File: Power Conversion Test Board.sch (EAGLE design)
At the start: 44 parts, among them U1 LM2678, U2 LM2678

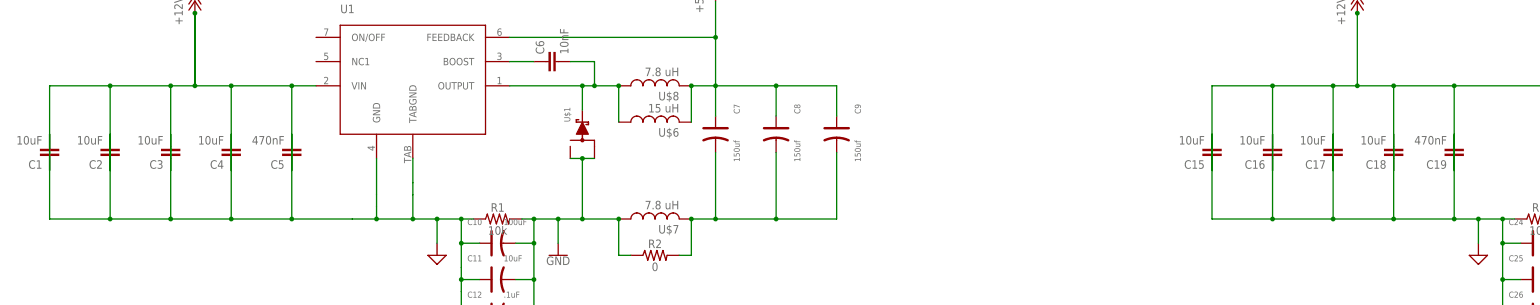
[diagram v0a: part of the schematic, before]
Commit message: Changed schematic layout and starting routing
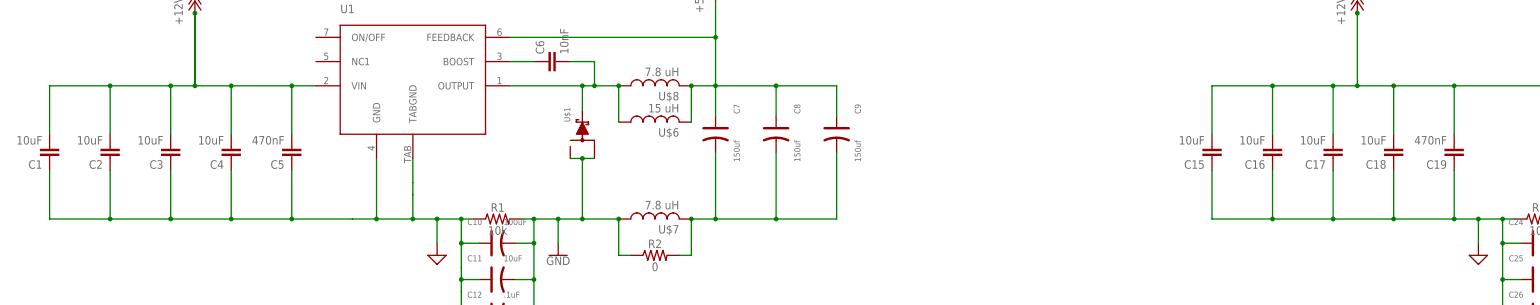
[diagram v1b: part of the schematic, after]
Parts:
- C1, C15, C16, C17, C18, C2, C3, C4: device SparkFun-Capacitors:10UF-0603-6.3V-20% -> SparkFun-Capacitors:10UF-1206-6.3V-20%
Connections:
- net +12V: now also C1.2, C15.2, C16.2, C17.2, C18.2, C19.2, C2.2, C3.2, C4.2, C5.2; no longer C1.1, C15.1, C16.1, C17.1, C18.1, C19.1, C2.1, C3.1, C4.1, C5.1
- net GND: now also C1.1, C15.1, C16.1, C17.1, C18.1, C19.1, C2.1, C3.1, C4.1, C5.1; no longer C1.2, C15.2, C16.2, C17.2, C18.2, C19.2, C2.2, C3.2, C4.2, C5.2

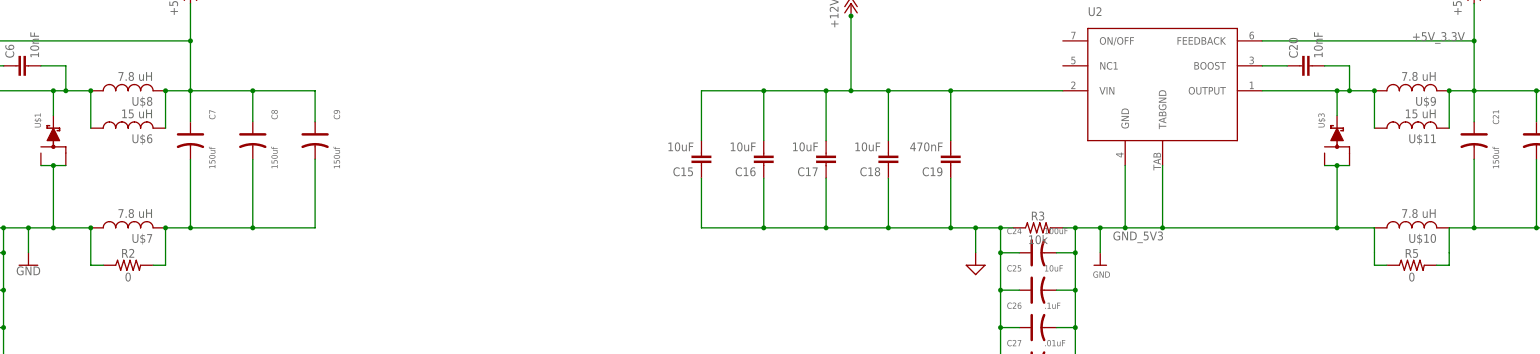
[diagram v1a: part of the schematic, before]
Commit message: Rerouting
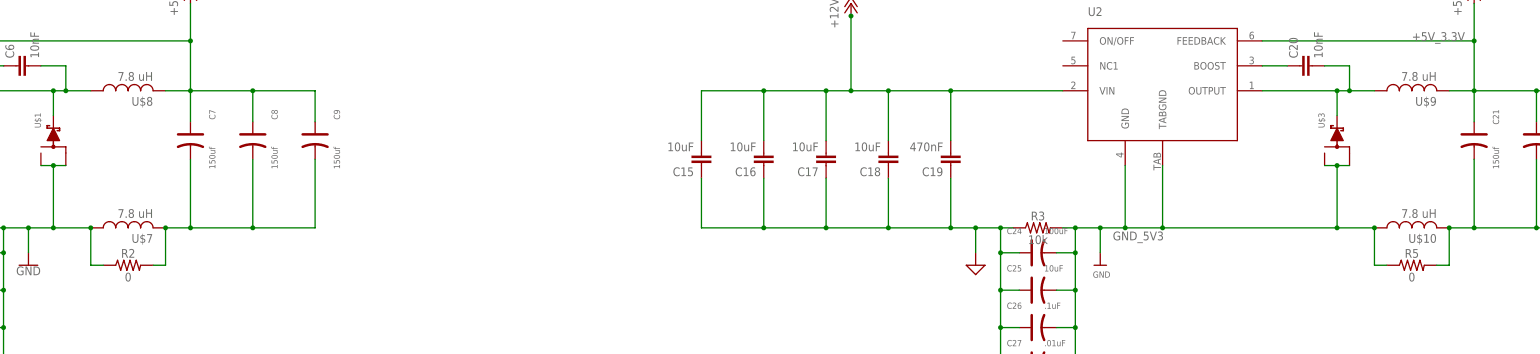
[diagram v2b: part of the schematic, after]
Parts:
- removed U$11, U$6: 15 uH, DiscreteComponents:HCMA1305
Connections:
- removed net GND_5V1: R5.1
- removed net N$6: C21.-, C22.-, C23.-, U$10.2
- net +5V: no longer U$6.2
- net +5V_3.3V: no longer U$11.2
- net GND_5V3: now also R5.1
- net N$1: no longer U$6.1
- net N$4: now also C21.-, C22.-, C23.-, U$10.2
- net N$7: no longer U$11.1
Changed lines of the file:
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@@
 <part name="U$2" library="microbuilder" deviceset="GND" device=""/>
 <part name="R2" library="SparkFun-Resistors" library_urn="urn:adsk.eagle:library:532" deviceset="RESISTOR" device="0603" package3d_urn="urn:adsk.eagle:package:39650/1" value="0"/>
-<part name="R5" library="SparkFun-Resistors" library_urn="urn:adsk.eagle:library:532" deviceset="RESISTOR" device="0603" package3d_urn="urn:adsk.eagle:package:39650/1" value="0"/>
 <part name="U$5" library="board_outlines" deviceset="BOARD" device="PCB"/>
 <part name="U$8" library="DiscreteComponents" deviceset="HCMA1305" device="" value="7.8 uH"/>
 <part name="U$9" library="DiscreteComponents" deviceset="HCMA1305" device="" value="7.8 uH"/>
 <part name="U$10" library="DiscreteComponents" deviceset="HCMA1305" device="" value="7.8 uH"/>
-<part name="U$11" library="DiscreteComponents" deviceset="HCMA1305" device="" value="15 uH"/>
-<part name="U$6" library="DiscreteComponents" deviceset="HCMA1305" device="" value="15 uH"/>
 <part name="U$7" library="DiscreteComponents" deviceset="HCMA1305" device="" value="7.8 uH"/>
+<part name="R5" library="SparkFun-Resistors" library_urn="urn:adsk.eagle:library:532" deviceset="RESISTOR" device="0603" package3d_urn="urn:adsk.eagle:package:39650/1" value="0"/>
 </parts>
 <sheets>
@@
 <attribute name="VALUE" x="203.2" y="105.156" size="1.778" layer="96" font="vector" align="top-center"/>
 </instance>
-<instance part="R5" gate="G$1" x="464.82" y="106.68">
-<attribute name="NAME" x="464.82" y="108.204" size="1.778" layer="95" font="vector" align="bottom-center"/>
-<attribute name="VALUE" x="464.82" y="105.156" size="1.778" layer="96" font="vector" align="top-center"/>
-</instance>
 <instance part="U$5" gate="G$1" x="246.38" y="35.56"/>
 <instance part="U$8" gate="G$1" x="203.2" y="142.24" rot="R90">
@@
 <attribute name="VALUE" x="469.9" y="118.11" size="1.778" layer="96" rot="R180"/>
 </instance>
-<instance part="U$11" gate="G$1" x="464.82" y="134.62" rot="R90">
-<attribute name="NAME" x="469.9" y="133.35" size="1.778" layer="95" rot="R180"/>
-<attribute name="VALUE" x="469.9" y="138.43" size="1.778" layer="96" rot="R180"/>
-</instance>
-<instance part="U$6" gate="G$1" x="203.2" y="134.62" rot="R90">
-<attribute name="NAME" x="208.28" y="133.35" size="1.778" layer="95" rot="R180"/>
-<attribute name="VALUE" x="208.28" y="138.43" size="1.778" layer="96" rot="R180"/>
-</instance>
 <instance part="U$7" gate="G$1" x="203.2" y="114.3" rot="R90">
 <attribute name="NAME" x="208.28" y="113.03" size="1.778" layer="95" rot="R180"/>
 <attribute name="VALUE" x="208.28" y="118.11" size="1.778" layer="96" rot="R180"/>
+</instance>
+<instance part="R5" gate="G$1" x="464.82" y="106.68">
+<attribute name="NAME" x="464.82" y="108.204" size="1.778" layer="95" font="vector" align="bottom-center"/>
+<attribute name="VALUE" x="464.82" y="105.156" size="1.778" layer="96" font="vector" align="top-center"/>
 </instance>
 </instances>
@@
 <wire x1="172.72" y1="152.4" x2="215.9" y2="152.4" width="0.1524" layer="91"/>
 <junction x="215.9" y="152.4"/>
-<wire x1="210.82" y1="142.24" x2="210.82" y2="134.62" width="0.1524" layer="91"/>
 <pinref part="U$8" gate="G$1" pin="2"/>
-<junction x="210.82" y="142.24"/>
-<pinref part="U$6" gate="G$1" pin="2"/>
 </segment>
 </net>
@@
 <wire x1="187.96" y1="137.16" x2="187.96" y2="142.24" width="0.1524" layer="91"/>
 <junction x="187.96" y="142.24"/>
-<wire x1="195.58" y1="142.24" x2="195.58" y2="134.62" width="0.1524" layer="91"/>
 <pinref part="U$8" gate="G$1" pin="1"/>
-<junction x="195.58" y="142.24"/>
-<pinref part="U$6" gate="G$1" pin="1"/>
 </segment>
 </net>
@@
 </segment>
 </net>
-<net name="N$6" class="0">
-<segment>
-<wire x1="502.92" y1="128.27" x2="502.92" y2="114.3" width="0.1524" layer="91"/>
-<wire x1="502.92" y1="114.3" x2="490.22" y2="114.3" width="0.1524" layer="91"/>
-<pinref part="C22" gate="G$1" pin="-"/>
-<wire x1="490.22" y1="114.3" x2="490.22" y2="128.27" width="0.1524" layer="91"/>
-<wire x1="490.22" y1="114.3" x2="477.52" y2="114.3" width="0.1524" layer="91"/>
-<junction x="490.22" y="114.3"/>
-<pinref part="C21" gate="G$1" pin="-"/>
-<wire x1="477.52" y1="114.3" x2="477.52" y2="128.27" width="0.1524" layer="91"/>
-<wire x1="477.52" y1="114.3" x2="472.44" y2="114.3" width="0.1524" layer="91"/>
-<junction x="477.52" y="114.3"/>
-<pinref part="C23" gate="G$1" pin="-"/>
-<pinref part="U$10" gate="G$1" pin="2"/>
-</segment>
-</net>
 <net name="N$7" class="0">
 <segment>
@@
 <wire x1="449.58" y1="137.16" x2="449.58" y2="142.24" width="0.1524" layer="91"/>
 <junction x="449.58" y="142.24"/>
-<wire x1="457.2" y1="142.24" x2="457.2" y2="134.62" width="0.1524" layer="91"/>
 <pinref part="U$9" gate="G$1" pin="1"/>
-<junction x="457.2" y="142.24"/>
-<pinref part="U$11" gate="G$1" pin="1"/>
 </segment>
 </net>
@@
 <junction x="477.52" y="152.4"/>
 <label x="464.82" y="152.4" size="1.778" layer="95"/>
-<wire x1="472.44" y1="134.62" x2="472.44" y2="142.24" width="0.1524" layer="91"/>
 <pinref part="U$9" gate="G$1" pin="2"/>
-<junction x="472.44" y="142.24"/>
-<pinref part="U$11" gate="G$1" pin="2"/>
 </segment>
 <segment>
@@
 <label x="403.86" y="111.76" size="1.778" layer="95"/>
 <pinref part="U$10" gate="G$1" pin="1"/>
+<wire x1="459.74" y1="106.68" x2="457.2" y2="106.68" width="0.1524" layer="91"/>
+<pinref part="R5" gate="G$1" pin="1"/>
+<wire x1="457.2" y1="114.3" x2="457.2" y2="106.68" width="0.1524" layer="91"/>
+<junction x="457.2" y="114.3"/>
 </segment>
 </net>
@@
 <net name="N$4" class="0">
 <segment>
-<wire x1="472.44" y1="114.3" x2="472.44" y2="109.22" width="0.1524" layer="91"/>
+<wire x1="469.9" y1="106.68" x2="472.44" y2="106.68" width="0.1524" layer="91"/>
 <pinref part="R5" gate="G$1" pin="2"/>
-<wire x1="469.9" y1="106.68" x2="472.44" y2="106.68" width="0.1524" layer="91"/>
-<wire x1="472.44" y1="106.68" x2="472.44" y2="109.22" width="0.1524" layer="91"/>
-</segment>
-</net>
-<net name="GND_5V1" class="0">
-<segment>
-<wire x1="457.2" y1="114.3" x2="457.2" y2="109.22" width="0.1524" layer="91"/>
-<pinref part="R5" gate="G$1" pin="1"/>
-<wire x1="459.74" y1="106.68" x2="457.2" y2="106.68" width="0.1524" layer="91"/>
-<wire x1="457.2" y1="106.68" x2="457.2" y2="109.22" width="0.1524" layer="91"/>
-</segment>
-</net>
+<wire x1="502.92" y1="128.27" x2="502.92" y2="114.3" width="0.1524" layer="91"/>
+<wire x1="502.92" y1="114.3" x2="490.22" y2="114.3" width="0.1524" layer="91"/>
+<pinref part="C22" gate="G$1" pin="-"/>
+<wire x1="490.22" y1="114.3" x2="490.22" y2="128.27" width="0.1524" layer="91"/>
+<wire x1="490.22" y1="114.3" x2="477.52" y2="114.3" width="0.1524" layer="91"/>
+<junction x="490.22" y="114.3"/>
+<pinref part="C21" gate="G$1" pin="-"/>
+<wire x1="477.52" y1="114.3" x2="477.52" y2="128.27" width="0.1524" layer="91"/>
+<wire x1="477.52" y1="114.3" x2="472.44" y2="114.3" width="0.1524" layer="91"/>
+<junction x="477.52" y="114.3"/>
+<pinref part="C23" gate="G$1" pin="-"/>
+<pinref part="U$10" gate="G$1" pin="2"/>
+<wire x1="472.44" y1="106.68" x2="472.44" y2="114.3" width="0.1524" layer="91"/>
+<junction x="472.44" y="114.3"/>
+</segment>
+</net>

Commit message: Repositioned the components of the board to get ready for tracing
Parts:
- added J1, J2, J3, J4: (no value), SparkFun-Connectors:BANANA_CONN
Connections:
- removed net GND: C1.1, C10.+, C11.+, C12.+, C13.+, C15.1, C16.1, C17.1, C18.1, C19.1, C2.1, C24.+, C25.+, C26.+, C27.+, C3.1, C4.1, C5.1, R1.1, R3.1, U1.GND, U1.TABGND
- removed net GND_5V: C10.-, C11.-, C12.-, C13.-, R1.2, R2.1, U$1.P$1, U$1.P$3, U$7.1
- removed net GND_5V3: C24.-, C25.-, C26.-, C27.-, R3.2, R5.1, U$10.1, U$3.P$1, U$3.P$3, U2.GND, U2.TABGND
- removed net N$9: R4.1, U$4.GND
- new net 12VGND: C1.1, C10.+, C11.+, C12.+, C13.+, C2.1, C3.1, C4.1, C5.1, J2.1, R1.1, U1.GND, U1.TABGND
- new net 3.3VGND: J4.1, R4.1, U$4.GND
- new net 5VGND: C10.-, C11.-, C12.-, C13.-, C24.-, C25.-, C26.-, C27.-, J3.1, R1.2, R2.1, R3.2, R5.1, U$1.P$1, U$1.P$3, U$10.1, U$3.P$1, U$3.P$3, U$7.1, U2.GND, U2.TABGND
- new net N$6: C15.1, C16.1, C17.1, C18.1, C19.1, C24.+, C25.+, C26.+, C27.+, R3.1
- net +12V: now also J1.1

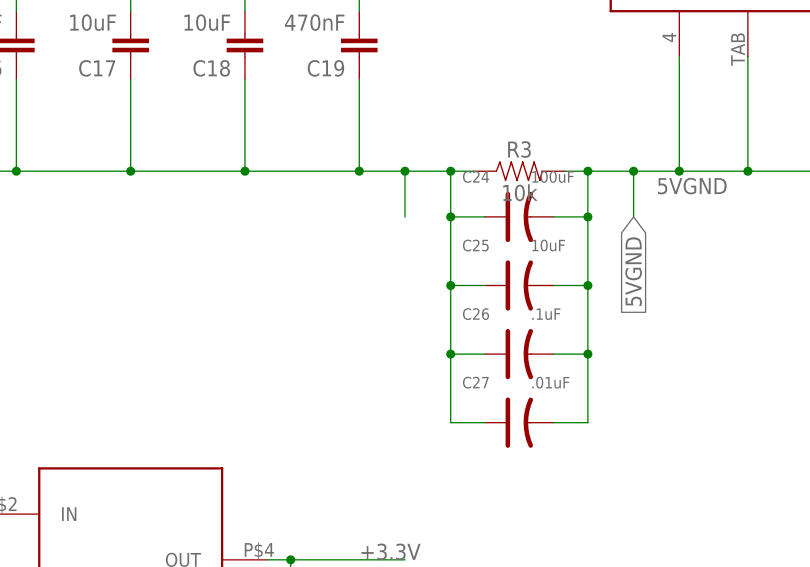
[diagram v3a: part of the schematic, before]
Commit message: re-positioned parts
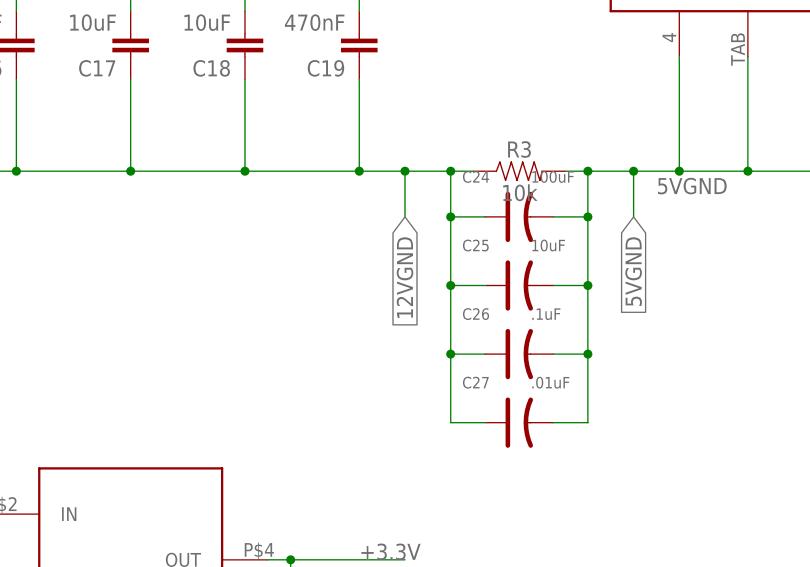
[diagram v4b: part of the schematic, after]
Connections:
- removed net N$6: C15.1, C16.1, C17.1, C18.1, C19.1, C24.+, C25.+, C26.+, C27.+, R3.1
- net 12VGND: now also C15.1, C16.1, C17.1, C18.1, C19.1, C24.+, C25.+, C26.+, C27.+, R3.1
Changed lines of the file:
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@@
-</segment>
-</net>
-<net name="N$6" class="0">
-<segment>
-<pinref part="C27" gate="G$1" pin="+"/>
-<pinref part="R3" gate="G$1" pin="1"/>
-<wire x1="375.92" y1="109.22" x2="375.92" y2="114.3" width="0.1524" layer="91"/>
-<wire x1="375.92" y1="114.3" x2="381" y2="114.3" width="0.1524" layer="91"/>
-<wire x1="381" y1="114.3" x2="383.54" y2="114.3" width="0.1524" layer="91"/>
-<junction x="381" y="114.3"/>
-<wire x1="381" y1="109.22" x2="381" y2="114.3" width="0.1524" layer="91"/>
-<pinref part="C24" gate="G$1" pin="+"/>
-<wire x1="384.81" y1="109.22" x2="381" y2="109.22" width="0.1524" layer="91"/>
-<junction x="381" y="109.22"/>
-<wire x1="381" y1="101.6" x2="381" y2="109.22" width="0.1524" layer="91"/>
-<pinref part="C25" gate="G$1" pin="+"/>
-<wire x1="384.81" y1="101.6" x2="381" y2="101.6" width="0.1524" layer="91"/>
-<junction x="381" y="101.6"/>
-<wire x1="381" y1="101.6" x2="381" y2="93.98" width="0.1524" layer="91"/>
-<pinref part="C26" gate="G$1" pin="+"/>
-<wire x1="384.81" y1="93.98" x2="381" y2="93.98" width="0.1524" layer="91"/>
-<junction x="381" y="93.98"/>
-<wire x1="381" y1="93.98" x2="381" y2="86.36" width="0.1524" layer="91"/>
-<wire x1="381" y1="86.36" x2="384.81" y2="86.36" width="0.1524" layer="91"/>
-<wire x1="320.04" y1="114.3" x2="332.74" y2="114.3" width="0.1524" layer="91"/>
-<wire x1="332.74" y1="114.3" x2="345.44" y2="114.3" width="0.1524" layer="91"/>
-<wire x1="345.44" y1="114.3" x2="358.14" y2="114.3" width="0.1524" layer="91"/>
-<wire x1="358.14" y1="114.3" x2="370.84" y2="114.3" width="0.1524" layer="91"/>
-<wire x1="375.92" y1="114.3" x2="370.84" y2="114.3" width="0.1524" layer="91"/>
-<junction x="375.92" y="114.3"/>
-<pinref part="C15" gate="G$1" pin="1"/>
-<wire x1="320.04" y1="124.46" x2="320.04" y2="114.3" width="0.1524" layer="91"/>
-<pinref part="C16" gate="G$1" pin="1"/>
-<wire x1="332.74" y1="124.46" x2="332.74" y2="114.3" width="0.1524" layer="91"/>
-<junction x="332.74" y="114.3"/>
-<pinref part="C17" gate="G$1" pin="1"/>
-<wire x1="345.44" y1="124.46" x2="345.44" y2="114.3" width="0.1524" layer="91"/>
-<junction x="345.44" y="114.3"/>
-<pinref part="C18" gate="G$1" pin="1"/>
-<wire x1="358.14" y1="124.46" x2="358.14" y2="114.3" width="0.1524" layer="91"/>
-<junction x="358.14" y="114.3"/>
-<pinref part="C19" gate="G$1" pin="1"/>
-<wire x1="370.84" y1="124.46" x2="370.84" y2="114.3" width="0.1524" layer="91"/>
-<junction x="370.84" y="114.3"/>
 </segment>
 </net>
@@
 <label x="66.04" y="96.52" size="1.778" layer="95" rot="R180" xref="yes"/>
 </segment>
+<segment>
+<pinref part="C27" gate="G$1" pin="+"/>
+<pinref part="R3" gate="G$1" pin="1"/>
+<wire x1="375.92" y1="109.22" x2="375.92" y2="114.3" width="0.1524" layer="91"/>
+<wire x1="375.92" y1="114.3" x2="381" y2="114.3" width="0.1524" layer="91"/>
+<wire x1="381" y1="114.3" x2="383.54" y2="114.3" width="0.1524" layer="91"/>
+<junction x="381" y="114.3"/>
+<wire x1="381" y1="109.22" x2="381" y2="114.3" width="0.1524" layer="91"/>
+<pinref part="C24" gate="G$1" pin="+"/>
+<wire x1="384.81" y1="109.22" x2="381" y2="109.22" width="0.1524" layer="91"/>
+<junction x="381" y="109.22"/>
+<wire x1="381" y1="101.6" x2="381" y2="109.22" width="0.1524" layer="91"/>
+<pinref part="C25" gate="G$1" pin="+"/>
+<wire x1="384.81" y1="101.6" x2="381" y2="101.6" width="0.1524" layer="91"/>
+<junction x="381" y="101.6"/>
+<wire x1="381" y1="101.6" x2="381" y2="93.98" width="0.1524" layer="91"/>
+<pinref part="C26" gate="G$1" pin="+"/>
+<wire x1="384.81" y1="93.98" x2="381" y2="93.98" width="0.1524" layer="91"/>
+<junction x="381" y="93.98"/>
+<wire x1="381" y1="93.98" x2="381" y2="86.36" width="0.1524" layer="91"/>
+<wire x1="381" y1="86.36" x2="384.81" y2="86.36" width="0.1524" layer="91"/>
+<wire x1="320.04" y1="114.3" x2="332.74" y2="114.3" width="0.1524" layer="91"/>
+<wire x1="332.74" y1="114.3" x2="345.44" y2="114.3" width="0.1524" layer="91"/>
+<wire x1="345.44" y1="114.3" x2="358.14" y2="114.3" width="0.1524" layer="91"/>
+<wire x1="358.14" y1="114.3" x2="370.84" y2="114.3" width="0.1524" layer="91"/>
+<wire x1="375.92" y1="114.3" x2="370.84" y2="114.3" width="0.1524" layer="91"/>
+<junction x="375.92" y="114.3"/>
+<pinref part="C15" gate="G$1" pin="1"/>
+<wire x1="320.04" y1="124.46" x2="320.04" y2="114.3" width="0.1524" layer="91"/>
+<pinref part="C16" gate="G$1" pin="1"/>
+<wire x1="332.74" y1="124.46" x2="332.74" y2="114.3" width="0.1524" layer="91"/>
+<junction x="332.74" y="114.3"/>
+<pinref part="C17" gate="G$1" pin="1"/>
+<wire x1="345.44" y1="124.46" x2="345.44" y2="114.3" width="0.1524" layer="91"/>
+<junction x="345.44" y="114.3"/>
+<pinref part="C18" gate="G$1" pin="1"/>
+<wire x1="358.14" y1="124.46" x2="358.14" y2="114.3" width="0.1524" layer="91"/>
+<junction x="358.14" y="114.3"/>
+<pinref part="C19" gate="G$1" pin="1"/>
+<wire x1="370.84" y1="124.46" x2="370.84" y2="114.3" width="0.1524" layer="91"/>
+<junction x="370.84" y="114.3"/>
+<label x="375.92" y="109.22" size="1.778" layer="95" rot="R270" xref="yes"/>
+</segment>
 </net>
